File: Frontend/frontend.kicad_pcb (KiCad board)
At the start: 4 copper layers, 100 x 100.2 mm, 346 parts, among them J1 VOCM, J10 SWD, J11 APWR, J2 BNC, J3 UMC, J4 UMC, J5 VOCM, J6 BNC, J7 UMC, J8 UMC, J9 PCIEx4 EDGE, K1 HE3600, K2 EE2-5NU, K3 HE3600, K4 HE3600, K5 EE2-5NU, K6 HE3600, Q1 ULN2003AD, U1 MCP9700T-E/TT, U10 ADA4817-1ACPZ, U11 MAX4567EEE, U12 MAX4567EEE, U13 MAX4567EEE, U14 AD8003ACPZ, U15 LMH6552SD, U16 MC33078DGK, U17 MAX5725AAUP, U18 STM32F030C8T, U19 MC33078DGK, U2 ADA4817-1ACPZ, U20 MC33078DGK, U23 LM317S, U24 MCP9700T-E/TT, U25 L78M05CDT, U26 TLV70233DSE, U27 MCP9700T-E/TT, U28 MC79M05CDT, U3 MAX4567EEE, U4 MAX4567EEE, U5 MAX4567EEE, U6 AD8003ACPZ, U7 LMH6552SD, U8 MC33078DGK, U9 MCP9700T-E/TT

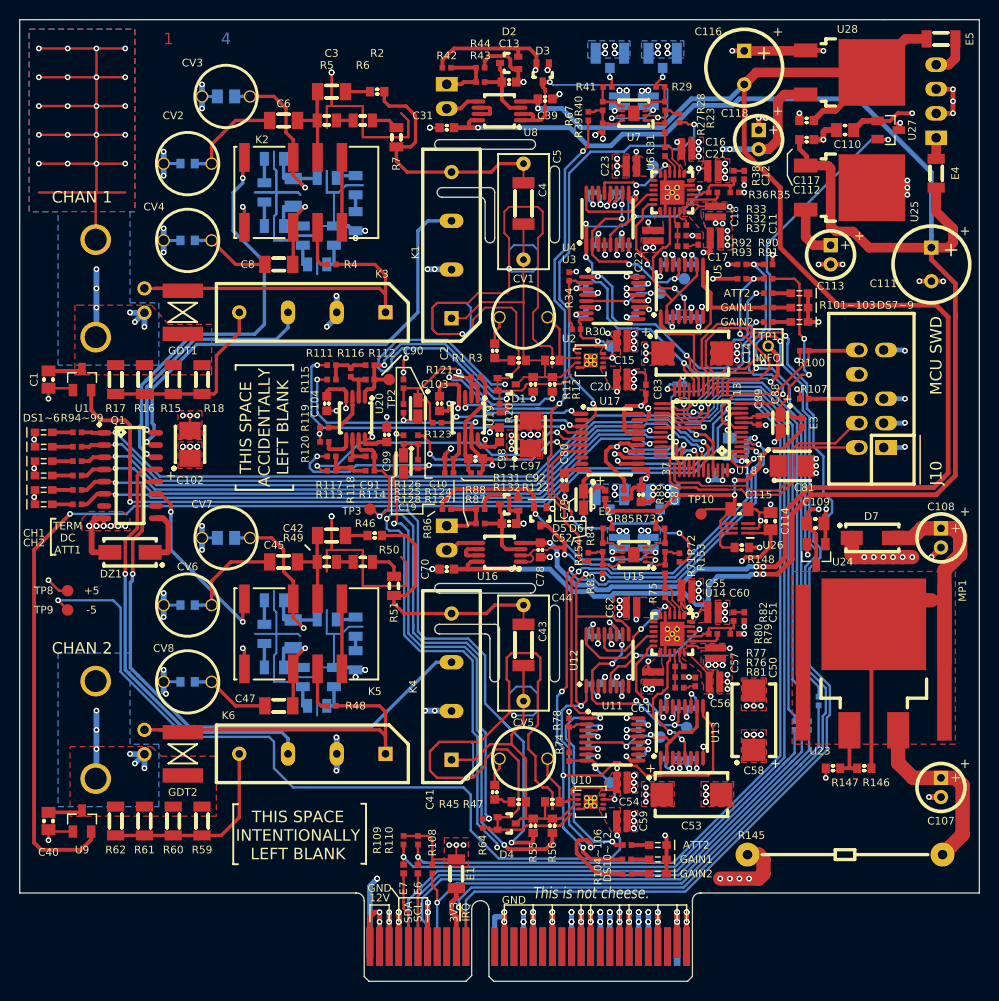
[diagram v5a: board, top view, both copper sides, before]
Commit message: Switch acq connectors to SATA
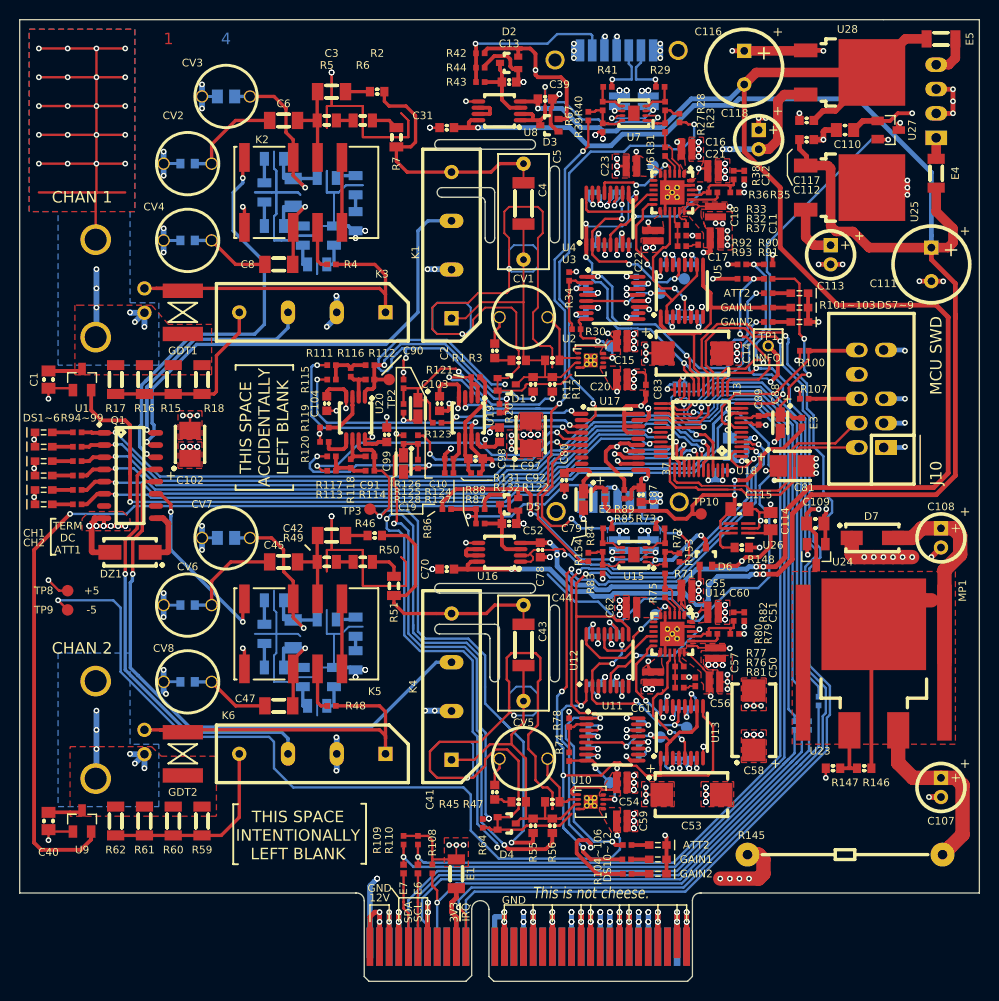
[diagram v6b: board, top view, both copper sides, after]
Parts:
- removed J4, J7, J8: UMC, conn-molex:CONN-MOLEX-0734120110
- removed J5: VOCM, conn-100mil:CONN-100MIL-M-1x2
- J1: value VOCM -> SATA; footprint conn-100mil:CONN-100MIL-M-1x2 -> conn-molex:CONN-MOLEX-0678005001
- J3: value UMC -> SATA; footprint conn-molex:CONN-MOLEX-0734120110 -> conn-molex:CONN-MOLEX-0678005001
- moved J3 47.0 mm to (124.3, 68.2), turned to 180 degrees
- moved J1 18.3 mm to (124.2, 21.2), turned to 180 degrees
- moved D6 17.8 mm to (133.5, 74.0), turned to 90 degrees
- moved D3 5.54 mm to (117.2, 29.0), turned to 180 degrees
- moved R42 3.81 mm to (110.0, 21.5), turned to 180 degrees
- moved C63 0.25 mm to (127.5, 72.8)
- moved C71 0.25 mm to (124.5, 72.8)
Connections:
- J1 pad 1: /Channel1/VOCM -> GND
- J1 pad 2: GND -> /Channel1/VO_P
- J3 pad 1: /Channel1/VO_P -> GND
- J3 pad 2: GND -> /Channel2/VO_P
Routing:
- net /Microcontroller/CH1_TEMP: track 84.4 -> 155.3 mm
- net /Channel2/VOCM: track 7.25 -> 20.8 mm, vias 0 -> 1
- net GND: track 1339.0 -> 1325.5 mm, vias 458 -> 437
- net /Channel1/VOCM: track 7.25 -> 18.2 mm, vias 0 -> 1
- net +5: track 515.4 -> 522.9 mm
- net /Channel1/VO_N: track 2.06 -> 5.97 mm
- net /Channel1/VO_P: track 2.26 -> 6.06 mm
- net /Channel2/VOS3: track 26.6 -> 29.8 mm
- net Net-(D6-Pad3): track 23.2 -> 26.4 mm, vias 2 -> 3
- net Net-(D3-Pad3): track 26.9 -> 23.8 mm
- net /Channel2/VO_N: track 2.06 -> 4.87 mm
- net /Channel2/VO_P: track 2.16 -> 4.75 mm
- net +3.3A: track 36.2 -> 35.0 mm
- net +2.5: track 70.6 -> 71.6 mm
- net -8: track 237.2 -> 238.2 mm
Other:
- board text removed: "N"
- board text removed: "P"
- board text removed: "Vocm DRIVE"

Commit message: More routing adjustments
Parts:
- removed R116, R118: 5k6, IPC7351-Nominal:RESC1005X40
- C3, C42, C46, C7: footprint IPC7351-Nominal:CAPC3216X70 -> smd-non-ipc:CAPC2828X260
- R1, R2, R45, R46: value 75 -> 64R9
- R119, R120, R121, R122, R131, R132: value 5k6 -> 3k3
- R146: value 120 -> 165
- R147: value 430 -> 620
- R27, R39, R71, R83: value 150 -> 220
- R28, R31, R40, R43, R72, R75, R84, R87: value 443 -> 442
- R4, R48: value 33 -> 35R7
- moved R86 1.52 mm to (108.0, 69.2), turned to 270 degrees
- moved R127 0.50 mm to (104.0, 64.2)
- moved R124 0.50 mm to (104.0, 61.8)
- moved R128 0.30 mm to (102.0, 61.5)
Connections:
- R111 pad 1: Net-(R111-Pad1) -> Net-(C90-Pad2)
- R112 pad 2: Net-(R111-Pad1) -> Net-(C90-Pad2)
- R113 pad 1: Net-(R113-Pad1) -> Net-(C91-Pad2)
- R114 pad 2: Net-(R113-Pad1) -> Net-(C91-Pad2)
- R115 pad 1: Net-(R111-Pad1) -> Net-(C90-Pad2)
- R117 pad 1: Net-(R113-Pad1) -> Net-(C91-Pad2)
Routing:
- net GND: track 1325.5 -> 1128.9 mm
- net /Microcontroller/CH1_TEMP: track 155.3 -> 83.9 mm
- net VRELAY: track 253.6 -> 239.4 mm, vias 16 -> 8
- net /Channel1/GUARD: track 97.6 -> 86.5 mm
- net /Channel2/GUARD: track 97.0 -> 86.7 mm
- net Net-(C46-Pad1): track 21.6 -> 15.2 mm, vias 1 -> 2
- net Net-(C7-Pad1): track 22.1 -> 15.9 mm
- net +5: track 522.9 -> 517.3 mm
- net Net-(R113-Pad1): track 5.25 -> 0.00 mm
- net Net-(R111-Pad1): track 4.85 -> 0.00 mm
- net Net-(C90-Pad2): track 3.48 -> 8.20 mm
- net Net-(C91-Pad2): track 3.85 -> 7.90 mm
- net +8: track 246.6 -> 243.5 mm, vias 10 -> 9
- net Net-(C46-Pad2): track 12.9 -> 10.8 mm, vias 1 -> 2
- net /Channel2/VOCM: track 20.8 -> 19.0 mm
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
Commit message: Update gerbers
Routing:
- net Net-(C7-Pad1): track 15.9 -> 18.4 mm
- net Net-(C46-Pad1): track 15.2 -> 17.7 mm
